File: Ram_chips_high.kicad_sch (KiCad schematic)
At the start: 10 parts, among them U25 MM5280, U26 MM5280, U27 MM5280, U28 MM5280, U40 MM5280, U41 MM5280, U42 MM5280, U43 MM5280, U6 74LS04, U7 74LS173

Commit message: Various corrections. Add new symbols and footprints
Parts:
- U25, U26, U27, U28, U40, U41, U42, U43: footprint (none) -> K-1008:DIP-22_W10.16mm_LongPads
- U6: footprint (none) -> K-1008:DIP-14_W7.62mm_LongPads
- U7: footprint (none) -> K-1008:DIP-16_W7.62mm_LongPads
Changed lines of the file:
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@@
       (effects (font (size 1.27 1.27)))
     )
-    (property "Footprint" "" (at 43.307 195.072 0)
+    (property "Footprint" "K-1008:DIP-14_W7.62mm_LongPads" (at 43.307 195.072 0)
       (effects (font (size 1.27 1.27)) hide)
     )
@@
       (effects (font (size 1.27 1.27)))
     )
-    (property "Footprint" "" (at 148.844 89.662 0)
+    (property "Footprint" "K-1008:DIP-22_W10.16mm_LongPads" (at 148.844 89.662 0)
       (effects (font (size 1.27 1.27)) hide)
     )
@@
     (pin "14")
     (pin "15")
+    (pin "16")
     (pin "17")
     (pin "19")
@@
       (effects (font (size 1.27 1.27)))
     )
-    (property "Footprint" "" (at 86.36 145.034 0)
+    (property "Footprint" "K-1008:DIP-22_W10.16mm_LongPads" (at 86.36 145.034 0)
       (effects (font (size 1.27 1.27)) hide)
     )
@@
     (pin "14")
     (pin "15")
+    (pin "16")
     (pin "17")
     (pin "19")
@@
       (effects (font (size 1.27 1.27)))
     )
-    (property "Footprint" "" (at 86.36 34.29 0)
+    (property "Footprint" "K-1008:DIP-22_W10.16mm_LongPads" (at 86.36 34.29 0)
       (effects (font (size 1.27 1.27)) hide)
     )
@@
     (pin "14")
     (pin "15")
+    (pin "16")
     (pin "17")
     (pin "19")
@@
       (effects (font (size 1.27 1.27)))
     )
-    (property "Footprint" "" (at 43.307 205.232 0)
+    (property "Footprint" "K-1008:DIP-14_W7.62mm_LongPads" (at 43.307 205.232 0)
       (effects (font (size 1.27 1.27)) hide)
     )
@@
       (effects (font (size 1.27 1.27)))
     )
-    (property "Footprint" "" (at 43.307 225.552 0)
+    (property "Footprint" "K-1008:DIP-14_W7.62mm_LongPads" (at 43.307 225.552 0)
       (effects (font (size 1.27 1.27)) hide)
     )
@@
       (effects (font (size 1.27 1.27)))
     )
-    (property "Footprint" "" (at 148.844 145.034 0)
+    (property "Footprint" "K-1008:DIP-22_W10.16mm_LongPads" (at 148.844 145.034 0)
       (effects (font (size 1.27 1.27)) hide)
     )
@@
     (pin "14")
     (pin "15")
+    (pin "16")
     (pin "17")
     (pin "19")
@@
       (effects (font (size 1.27 1.27)))
     )
-    (property "Footprint" "" (at 148.844 200.406 0)
+    (property "Footprint" "K-1008:DIP-22_W10.16mm_LongPads" (at 148.844 200.406 0)
       (effects (font (size 1.27 1.27)) hide)
     )
@@
     (pin "14")
     (pin "15")
+    (pin "16")
     (pin "17")
     (pin "19")
@@
       (effects (font (size 1.27 1.27)))
     )
-    (property "Footprint" "" (at 148.844 34.29 0)
+    (property "Footprint" "K-1008:DIP-22_W10.16mm_LongPads" (at 148.844 34.29 0)
       (effects (font (size 1.27 1.27)) hide)
     )
@@
     (pin "14")
     (pin "15")
+    (pin "16")
     (pin "17")
     (pin "19")
@@
       (effects (font (size 1.27 1.27)))
     )
-    (property "Footprint" "" (at 43.307 215.392 0)
+    (property "Footprint" "K-1008:DIP-14_W7.62mm_LongPads" (at 43.307 215.392 0)
       (effects (font (size 1.27 1.27)) hide)
     )
@@
       (effects (font (size 1.27 1.27)))
     )
-    (property "Footprint" "" (at 86.36 200.406 0)
+    (property "Footprint" "K-1008:DIP-22_W10.16mm_LongPads" (at 86.36 200.406 0)
       (effects (font (size 1.27 1.27)) hide)
     )
@@
     (pin "14")
     (pin "15")
+    (pin "16")
     (pin "17")
     (pin "19")
@@
       (effects (font (size 1.27 1.27)))
     )
-    (property "Footprint" "" (at 86.36 89.662 0)
+    (property "Footprint" "K-1008:DIP-22_W10.16mm_LongPads" (at 86.36 89.662 0)
       (effects (font (size 1.27 1.27)) hide)
     )
@@
     (pin "14")
     (pin "15")
+    (pin "16")
     (pin "17")
     (pin "19")
@@
       (effects (font (size 1.27 1.27)))
     )
-    (property "Footprint" "" (at 62.738 253.746 0)
-      (effects (font (size 1.27 1.27)) hide)
-    )
+    (property "Footprint" "K-1008:DIP-16_W7.62mm_LongPads" (at 62.738 253.746 0)
+      (effects (font (size 1.27 1.27)) hide)
+    )

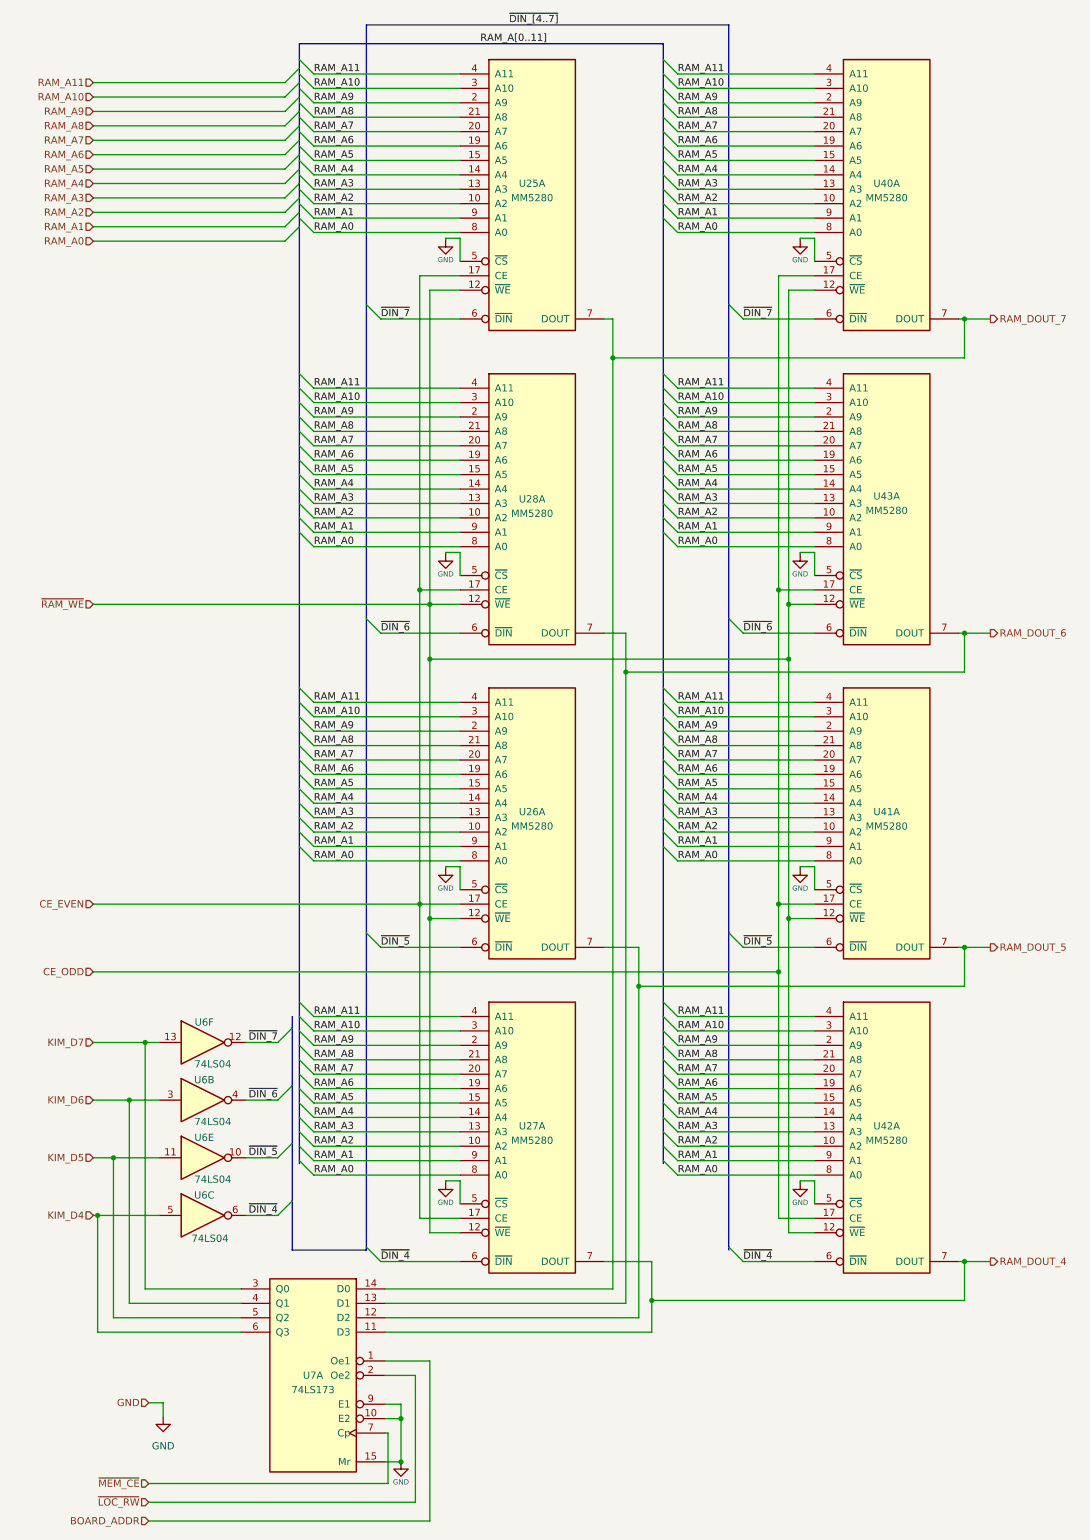
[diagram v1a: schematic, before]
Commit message: Correct address bus connections
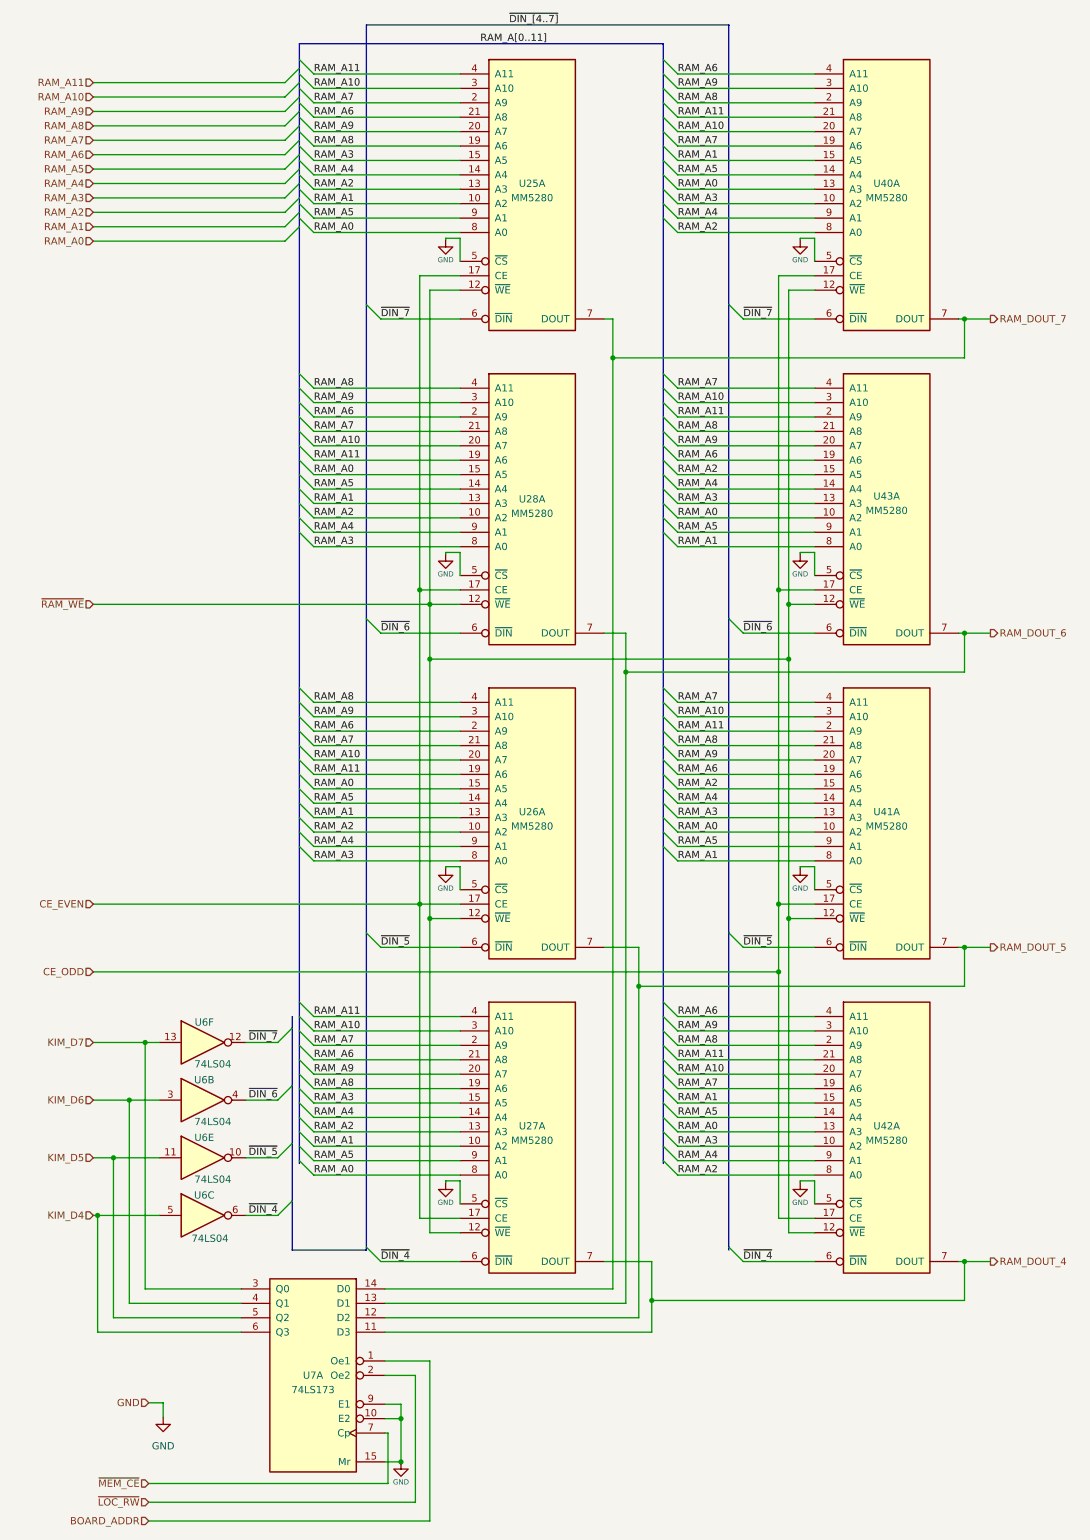
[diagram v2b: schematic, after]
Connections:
- net RAM_A0: now also U26.15 (A5), U28.15 (A5), U40.13 (A3), U41.10 (A2), U42.13 (A3), U43.10 (A2); no longer U26.8 (A0), U28.8 (A0), U40.8 (A0), U41.8 (A0), U42.8 (A0), U43.8 (A0)
- net RAM_A1: now also U25.10 (A2), U26.13 (A3), U27.10 (A2), U28.13 (A3), U40.15 (A5), U41.8 (A0), U42.15 (A5), U43.8 (A0); no longer U25.9 (A1), U26.9 (A1), U27.9 (A1), U28.9 (A1), U40.9 (A1), U41.9 (A1), U42.9 (A1), U43.9 (A1)
- net RAM_A10: now also U26.20 (A7), U28.20 (A7), U40.20 (A7), U42.20 (A7); no longer U26.3 (A10), U28.3 (A10), U40.3 (A10), U42.3 (A10)
- net RAM_A11: now also U26.19 (A6), U28.19 (A6), U40.21 (A8), U41.2 (A9), U42.21 (A8), U43.2 (A9); no longer U26.4 (A11), U28.4 (A11), U40.4 (A11), U41.4 (A11), U42.4 (A11), U43.4 (A11)
- net RAM_A2: now also U25.13 (A3), U27.13 (A3), U40.8 (A0), U41.15 (A5), U42.8 (A0), U43.15 (A5); no longer U25.10 (A2), U27.10 (A2), U40.10 (A2), U41.10 (A2), U42.10 (A2), U43.10 (A2)
- net RAM_A3: now also U25.15 (A5), U26.8 (A0), U27.15 (A5), U28.8 (A0), U40.10 (A2), U42.10 (A2); no longer U25.13 (A3), U26.13 (A3), U27.13 (A3), U28.13 (A3), U40.13 (A3), U42.13 (A3)
- net RAM_A4: now also U26.9 (A1), U28.9 (A1), U40.9 (A1), U42.9 (A1); no longer U26.14 (A4), U28.14 (A4), U40.14 (A4), U42.14 (A4)
- net RAM_A5: now also U25.9 (A1), U26.14 (A4), U27.9 (A1), U28.14 (A4), U40.14 (A4), U41.9 (A1), U42.14 (A4), U43.9 (A1); no longer U25.15 (A5), U26.15 (A5), U27.15 (A5), U28.15 (A5), U40.15 (A5), U41.15 (A5), U42.15 (A5), U43.15 (A5)
- net RAM_A6: now also U25.21 (A8), U26.2 (A9), U27.21 (A8), U28.2 (A9), U40.4 (A11), U42.4 (A11); no longer U25.19 (A6), U26.19 (A6), U27.19 (A6), U28.19 (A6), U40.19 (A6), U42.19 (A6)
- net RAM_A7: now also U25.2 (A9), U26.21 (A8), U27.2 (A9), U28.21 (A8), U40.19 (A6), U41.4 (A11), U42.19 (A6), U43.4 (A11); no longer U25.20 (A7), U26.20 (A7), U27.20 (A7), U28.20 (A7), U40.20 (A7), U41.20 (A7), U42.20 (A7), U43.20 (A7)
- net RAM_A8: now also U25.19 (A6), U26.4 (A11), U27.19 (A6), U28.4 (A11), U40.2 (A9), U42.2 (A9); no longer U25.21 (A8), U26.21 (A8), U27.21 (A8), U28.21 (A8), U40.21 (A8), U42.21 (A8)
- net RAM_A9: now also U25.20 (A7), U26.3 (A10), U27.20 (A7), U28.3 (A10), U40.3 (A10), U41.20 (A7), U42.3 (A10), U43.20 (A7); no longer U25.2 (A9), U26.2 (A9), U27.2 (A9), U28.2 (A9), U40.2 (A9), U41.2 (A9), U42.2 (A9), U43.2 (A9)
